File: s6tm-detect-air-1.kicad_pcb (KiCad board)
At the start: 2 copper layers, 67 x 67 mm, 82 parts, among them J1 Conn_01x04, J2 TC2030, J3 Conn_01x04, J4 Conn_01x04, J5 Conn_01x04_Pin, J6 Conn_01x08, SW1 SW_Push, SW2 SW_Push, U1 SYS1002-H2, U10 004-1-0100, U2 MiCS-5524, U3 LMC6482, U4 HT753-1, U5 SN65HVD230, U6 STM32F103C8Tx, U7 HTU21, U8 LM73100, U9 ENS16x, Y1 8M

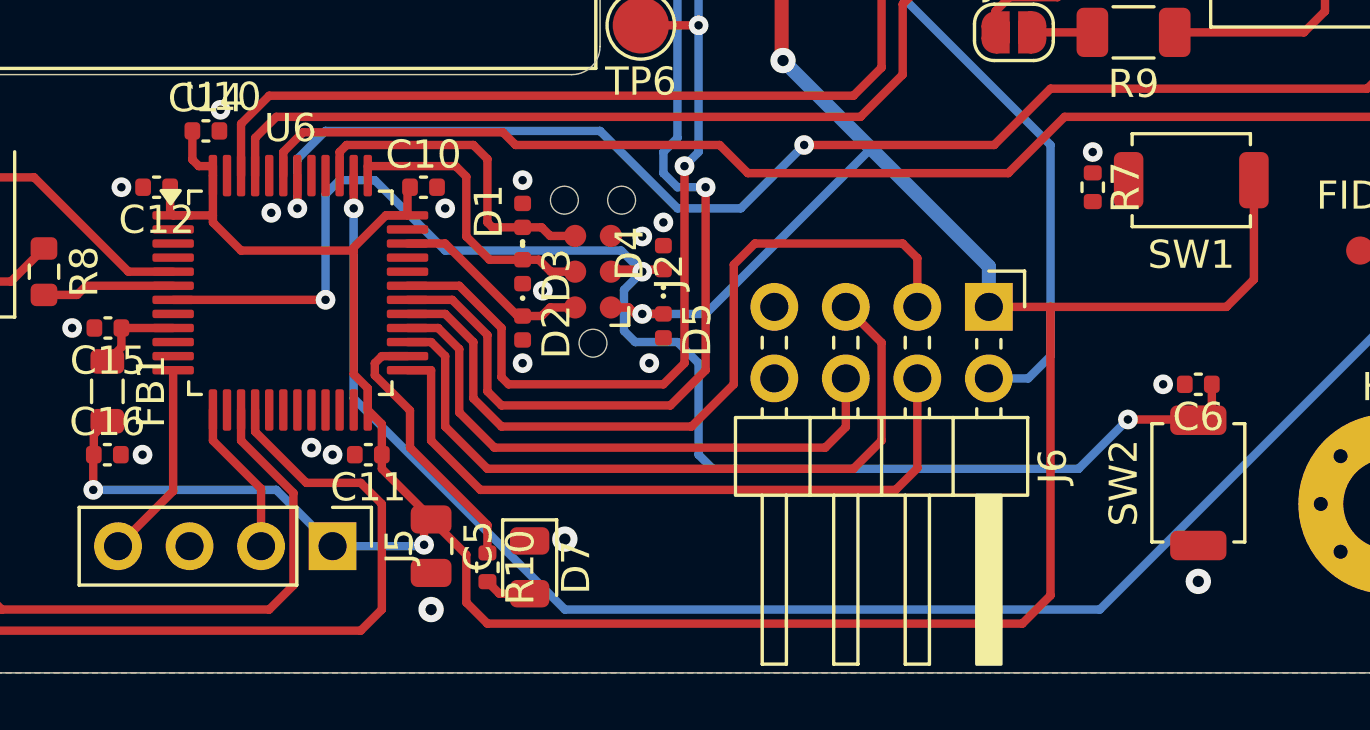
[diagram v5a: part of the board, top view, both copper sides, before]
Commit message: pcb: add boot routing
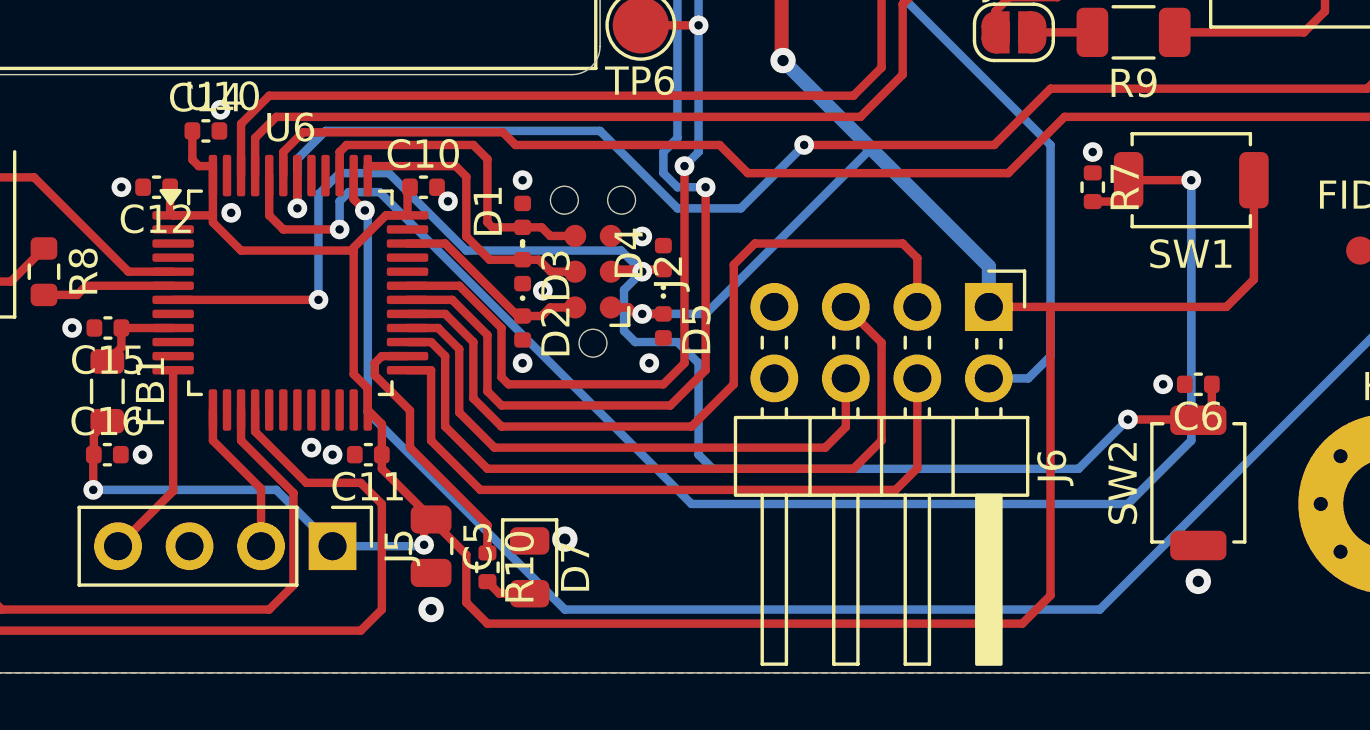
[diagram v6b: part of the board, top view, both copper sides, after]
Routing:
- net /BOOT: track 0.00 -> 54.8 mm, vias 0 -> 2
- net GND: vias 46 -> 45
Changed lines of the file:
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@@
 	)
 	(via
-		(at 142.5 103.5)
+		(at 142.6 103.25)
 		(size 0.7)
 		(drill 0.3)
@@
 	)
 	(via
-		(at 150.25 104)
-		(size 0.7)
-		(drill 0.3)
-		(layers "F.Cu" "B.Cu")
-		(free yes)
-		(net "GND")
-	)
-	(via
 		(at 166.25 86.75)
 		(size 0.7)
@@
 	)
 	(via
-		(at 136.323189 103.659869)
+		(at 134.9 103.659869)
 		(size 0.7)
 		(drill 0.3)
@@
 	)
 	(segment
+		(start 139.25 102.3375)
+		(end 139.25 103.175933)
+		(width 0.3)
+		(layer "F.Cu")
+		(net "/~{ENS_INT}")
+	)
+	(segment
 		(start 145.5 59.75)
 		(end 146.025 59.75)
@@
 	)
 	(segment
-		(start 139.25 102.3375)
-		(end 139.25 103.5)
+		(start 139.25 103.175933)
+		(end 139.648709 103.574642)
 		(width 0.3)
 		(layer "F.Cu")
@@
 	)
 	(via
-		(at 139.25 103.5)
+		(at 139.648709 103.574642)
 		(size 0.7)
 		(drill 0.3)
@@
 	)
 	(segment
-		(start 144.5 58.75)
-		(end 145.5 59.75)
+		(start 145.5 55.25)
+		(end 144.5 56.25)
 		(width 0.3)
 		(layer "B.Cu")
@@
 	)
 	(segment
-		(start 180 67.25)
-		(end 176.25 63.5)
+		(start 180 78.25)
+		(end 180 67.25)
 		(width 0.3)
 		(layer "B.Cu")
@@
 	)
 	(segment
-		(start 165.75 117.75)
-		(end 177 106.5)
+		(start 144.5 58.75)
+		(end 145.5 59.75)
 		(width 0.3)
 		(layer "B.Cu")
@@
 	)
 	(segment
-		(start 159.25 55.25)
-		(end 145.5 55.25)
+		(start 146.75 117.75)
+		(end 165.75 117.75)
 		(width 0.3)
 		(layer "B.Cu")
@@
 	)
 	(segment
-		(start 176.25 63.5)
-		(end 167.5 63.5)
+		(start 139.75 103.675933)
+		(end 139.75 110.75)
 		(width 0.3)
 		(layer "B.Cu")
@@
 	)
 	(segment
-		(start 139.25 110.25)
+		(start 139.75 110.75)
 		(end 146.75 117.75)
 		(width 0.3)
@@
 	)
 	(segment
+		(start 180 67.25)
+		(end 176.25 63.5)
+		(width 0.3)
+		(layer "B.Cu")
+		(net "/~{ENS_INT}")
+	)
+	(segment
 		(start 144.5 56.25)
 		(end 144.5 58.75)
@@
 	)
 	(segment
-		(start 180 78.25)
-		(end 180 67.25)
+		(start 167.5 63.5)
+		(end 159.25 55.25)
 		(width 0.3)
 		(layer "B.Cu")
@@
 	)
 	(segment
-		(start 145.5 55.25)
-		(end 144.5 56.25)
+		(start 159.25 55.25)
+		(end 145.5 55.25)
 		(width 0.3)
 		(layer "B.Cu")
@@
 	)
 	(segment
-		(start 139.25 103.5)
-		(end 139.25 110.25)
+		(start 139.648709 103.574642)
+		(end 139.75 103.675933)
 		(width 0.3)
 		(layer "B.Cu")
@@
 	)
 	(segment
-		(start 177 106.5)
-		(end 177 81.25)
+		(start 177 81.25)
+		(end 180 78.25)
 		(width 0.3)
 		(layer "B.Cu")
@@
 	)
 	(segment
-		(start 146.75 117.75)
-		(end 165.75 117.75)
+		(start 165.75 117.75)
+		(end 177 106.5)
 		(width 0.3)
 		(layer "B.Cu")
@@
 	)
 	(segment
-		(start 167.5 63.5)
-		(end 159.25 55.25)
+		(start 176.25 63.5)
+		(end 167.5 63.5)
 		(width 0.3)
 		(layer "B.Cu")
@@
 	)
 	(segment
-		(start 177 81.25)
-		(end 180 78.25)
+		(start 177 106.5)
+		(end 177 81.25)
 		(width 0.3)
 		(layer "B.Cu")
@@
 	(segment
 		(start 132.8375 106.75)
-		(end 138.25 106.75)
+		(end 138 106.75)
 		(width 0.3)
 		(layer "F.Cu")
@@
 	)
 	(via
-		(at 138.25 106.75)
+		(at 138 106.75)
 		(size 0.7)
 		(drill 0.3)
@@
 	)
 	(segment
-		(start 142.5 105)
-		(end 148.75 105)
+		(start 151.5 109)
+		(end 151.5 112.25)
 		(width 0.3)
 		(layer "B.Cu")
@@
 	)
 	(segment
-		(start 140 102.5)
-		(end 142.5 105)
+		(start 148.85 106.4)
+		(end 148.85 107.85)
 		(width 0.3)
 		(layer "B.Cu")
@@
 	)
 	(segment
-		(start 138.25 103)
-		(end 138.75 102.5)
+		(start 138 106.75)
+		(end 138 103)
 		(width 0.3)
 		(layer "B.Cu")
@@
 	)
 	(segment
-		(start 151.5 109)
-		(end 151.5 112.25)
+		(start 148.85 107.85)
+		(end 149.25 108.25)
 		(width 0.3)
 		(layer "B.Cu")
@@
 	)
 	(segment
-		(start 148.85 106.4)
-		(end 148.85 107.85)
+		(start 143.25 105)
+		(end 148.75 105)
 		(width 0.3)
 		(layer "B.Cu")
@@
 	)
 	(segment
-		(start 138.75 102.5)
-		(end 140 102.5)
+		(start 151.5 112.25)
+		(end 152 112.75)
 		(width 0.3)
 		(layer "B.Cu")
@@
 	)
 	(segment
-		(start 148.85 107.85)
-		(end 149.25 108.25)
+		(start 152 112.75)
+		(end 165 112.75)
 		(width 0.3)
 		(layer "B.Cu")
@@
 	)
 	(segment
-		(start 138.25 106.75)
-		(end 138.25 103)
+		(start 138.75 102.25)
+		(end 140.5 102.25)
 		(width 0.3)
 		(layer "B.Cu")
@@
 	)
 	(segment
-		(start 151.5 112.25)
-		(end 152 112.75)
+		(start 148.75 105)
+		(end 149.5 105.75)
 		(width 0.3)
 		(layer "B.Cu")
@@
 	)
 	(segment
-		(start 152 112.75)
-		(end 165 112.75)
+		(start 140.5 102.25)
+		(end 143.25 105)
 		(width 0.3)
 		(layer "B.Cu")
@@
 	)
 	(segment
-		(start 148.75 105)
-		(end 149.5 105.75)
+		(start 138 103)
+		(end 138.75 102.25)
 		(width 0.3)
 		(layer "B.Cu")
@@
 	)
 	(segment
+		(start 166.775 103.025)
+		(end 166.775 102.5)
+		(width 0.3)
+		(layer "F.Cu")
+		(net "/BOOT")
+	)
+	(segment
+		(start 136.75 104.25)
+		(end 138.75 104.25)
+		(width 0.3)
+		(layer "F.Cu")
+		(net "/BOOT")
+	)
+	(segment
+		(start 166.99 103.26)
+		(end 167 103.25)
+		(width 0.3)
+		(layer "F.Cu")
+		(net "/BOOT")
+	)
+	(segment
+		(start 165.5 103.26)
+		(end 166.99 103.26)
+		(width 0.3)
+		(layer "F.Cu")
+		(net "/BOOT")
+	)
+	(segment
+		(start 167 103.25)
+		(end 166.775 103.025)
+		(width 0.3)
+		(layer "F.Cu")
+		(net "/BOOT")
+	)
+	(segment
+		(start 136.25 103.75)
+		(end 136.75 104.25)
+		(width 0.3)
+		(layer "F.Cu")
+		(net "/BOOT")
+	)
+	(segment
+		(start 169 102.5)
+		(end 166.775 102.5)
+		(width 0.3)
+		(layer "F.Cu")
+		(net "/BOOT")
+	)
+	(segment
+		(start 136.25 102.3375)
+		(end 136.25 103.75)
+		(width 0.3)
+		(layer "F.Cu")
+		(net "/BOOT")
+	)
+	(via
+		(at 169 102.5)
+		(size 0.7)
+		(drill 0.3)
+		(layers "F.Cu" "B.Cu")
+		(net "/BOOT")
+	)
+	(via
+		(at 138.75 104.25)
+		(size 0.7)
+		(drill 0.3)
+		(layers "F.Cu" "B.Cu")
+		(net "/BOOT")
+	)
+	(segment
+		(start 151.25 114)
+		(end 166.75 114)
+		(width 0.3)
+		(layer "B.Cu")
+		(net "/BOOT")
+	)
+	(segment
+		(start 138.75 104.25)
+		(end 138.75 103.25)
+		(width 0.3)
+		(layer "B.Cu")
+		(net "/BOOT")
+	)
+	(segment
+		(start 138.75 103.25)
+		(end 139.075358 102.924642)
+		(width 0.3)
+		(layer "B.Cu")
+		(net "/BOOT")
+	)
+	(segment
+		(start 166.75 114)
+		(end 169 111.75)
+		(width 0.3)
+		(layer "B.Cu")
+		(net "/BOOT")
+	)
+	(segment
+		(start 140.174642 102.924642)
+		(end 151.25 114)
+		(width 0.3)
+		(layer "B.Cu")
+		(net "/BOOT")
+	)
+	(segment
+		(start 169 111.75)
+		(end 169 102.5)
+		(width 0.3)
+		(layer "B.Cu")
+		(net "/BOOT")
+	)
+	(segment
+		(start 139.075358 102.924642)
+		(end 140.174642 102.924642)
+		(width 0.3)
+		(layer "B.Cu")
+		(net "/BOOT")
+	)
+	(segment

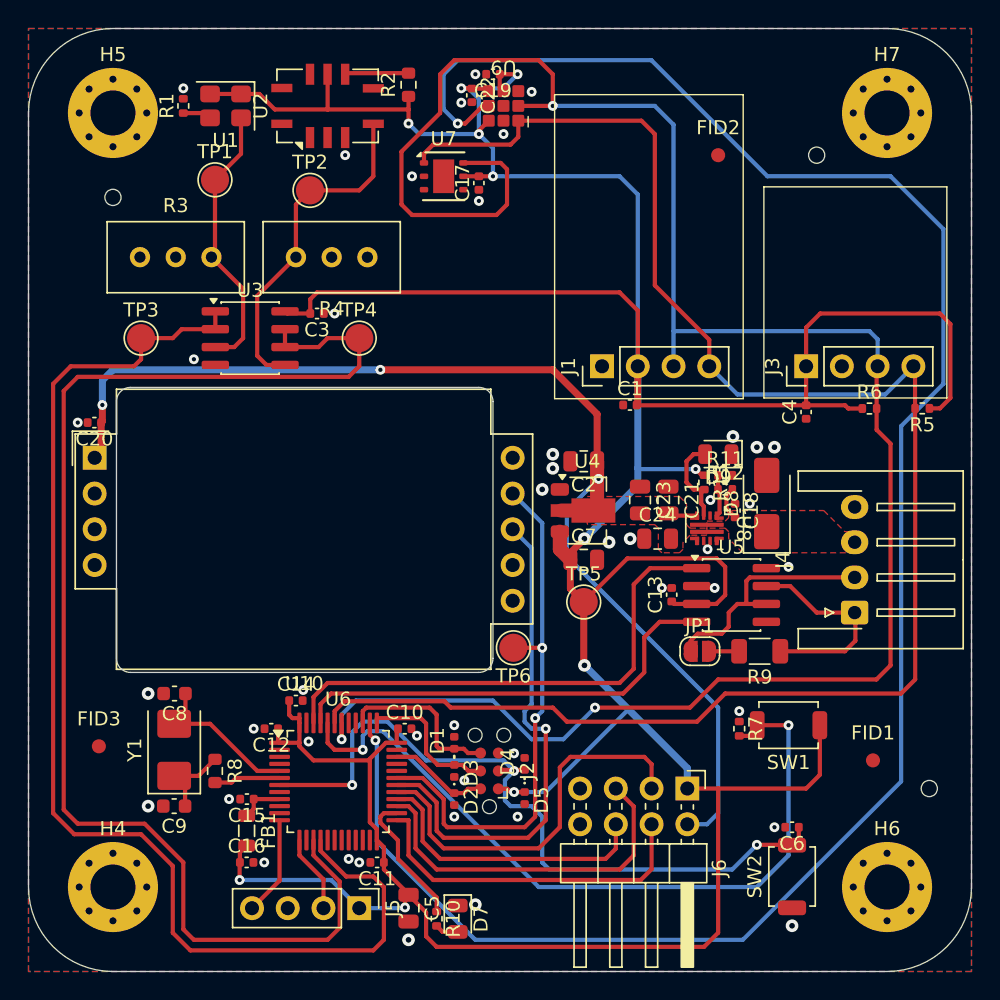
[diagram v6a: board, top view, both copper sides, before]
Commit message: pcb: add stitching vias
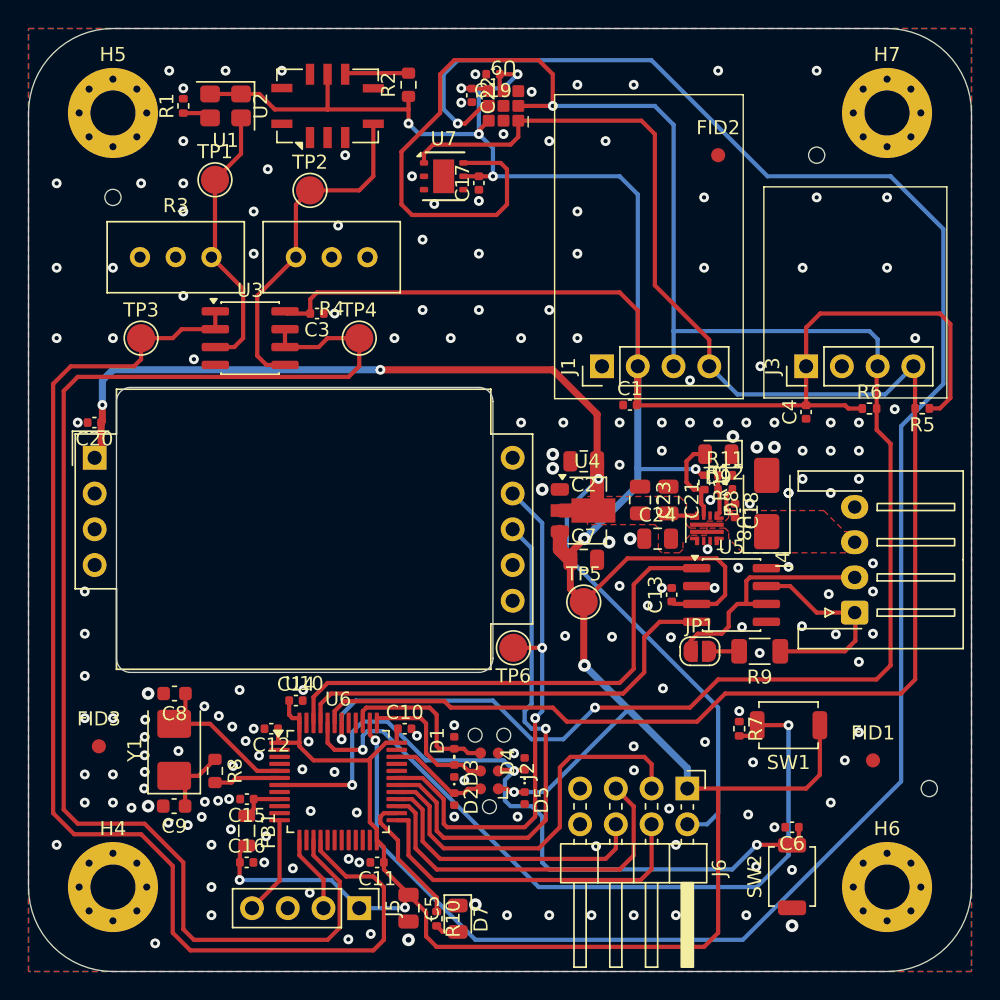
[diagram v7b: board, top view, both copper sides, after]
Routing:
- net +3V3: track 304.0 -> 303.2 mm
- net GND: vias 45 -> 188
